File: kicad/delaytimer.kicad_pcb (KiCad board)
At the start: 2 copper layers, 39.6 x 33.3 mm, 21 parts, among them P1 CONN_01X04, Q1 MMBT3904, Q2 MMBT3904, Q3 MMBT3906, Q4 MMBT3906, Q5 IRLML6344, U1 NE555

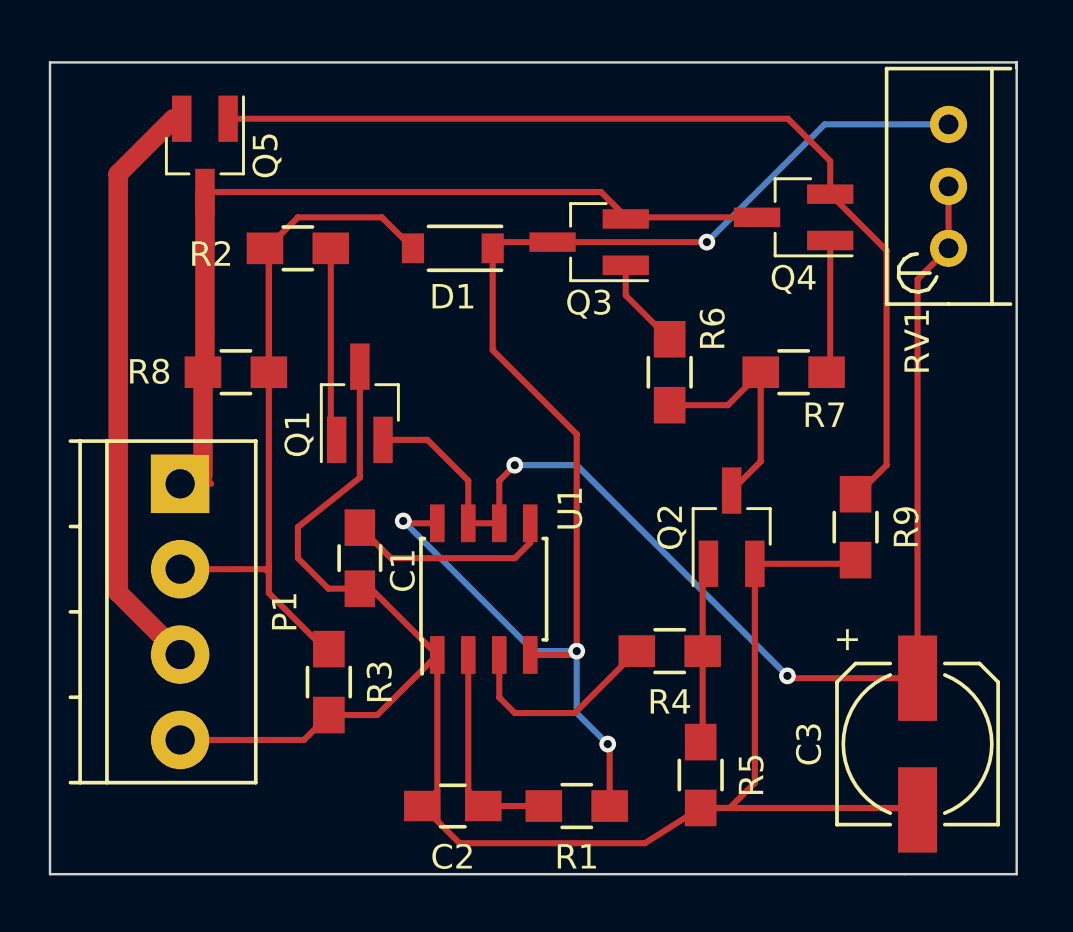
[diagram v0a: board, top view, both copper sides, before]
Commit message: Update schema / pcb / readme
- Removed unneeded resistor
- Reduce vias
- Fix labels for header
- Added copper pour on front/back
- UpdatedBOM
- Added Makefile for building BOM CSV
- Update README
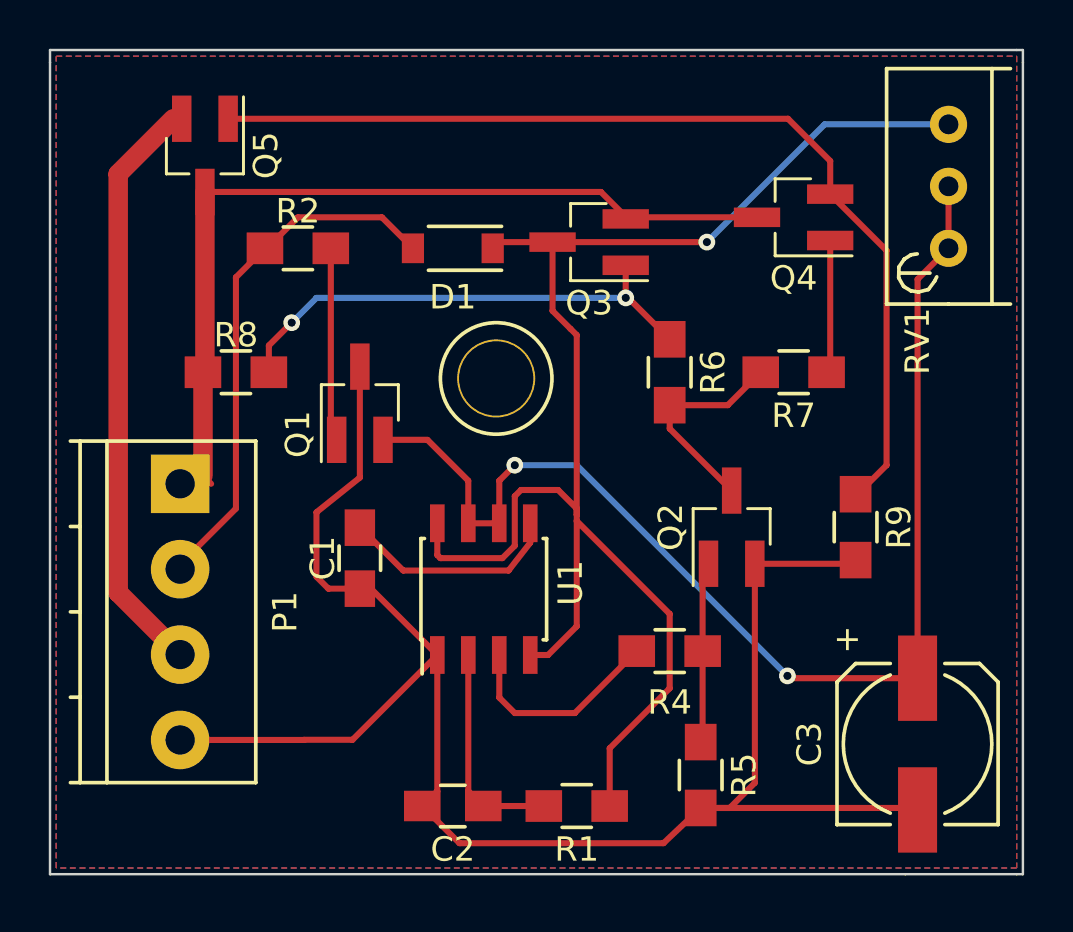
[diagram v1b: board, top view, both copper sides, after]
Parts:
- removed R3: 10k, Resistors_SMD:R_0805_HandSoldering
- added ?: , Connectors:1pin, F.Cu at (147.8, 93.0)
- R2: value 100k -> 2.2k
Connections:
- R8 pad 2: Switched12V -> Net-(Q3-Pad1)
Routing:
- net Net-(Q3-Pad1): track 3.78 -> 21.1 mm, vias 0 -> 2
- net Switched12V: track 33.6 -> 22.2 mm
- net VCC: track 59.2 -> 64.3 mm, vias 4 -> 1
- net Net-(Q2-Pad3): track 9.63 -> 8.84 mm
- net GND: track 72.1 -> 71.5 mm
- net Net-(C1-Pad1): track 8.56 -> 9.07 mm
- added copper zone on B.Cu, net GND
- added copper zone on F.Cu, net GND
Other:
- board size 39.6 x 33.3 mm -> 39.9 x 33.8 mm
- rule trace_min: 0.25 -> 0.1524
- board text added: "5-12V"
- board text added: "Output"
- board text added: "Switch"
- board text removed: "In12V"
- board text removed: "Out12V"
- board text removed: "Switch12V"

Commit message: Add static resistor option in place of pot
- Added a static resistor (ROpt) so you can save on the price of a pot
- Added measurements to the board for making an enclosure
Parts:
- added ROpt: 100k, Resistors_SMD:R_0805_HandSoldering, F.Cu at (160.3, 100.6)
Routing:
- net VCC: track 64.3 -> 75.5 mm
- net Net-(C3-Pad1): track 50.7 -> 54.1 mm
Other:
- board text added: "Ropt =Static Timer"
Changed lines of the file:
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@@
 (kicad_pcb (version 4) (host pcbnew 4.0.5)
   (general
-    (links 39)
-    (no_connects 0)
+    (links 43)
+    (no_connects 2)
     (area 129.489999 79.451999 169.468001 113.334001)
     (thickness 1.6002)
-    (drawings 14)
-    (tracks 135)
+    (drawings 24)
+    (tracks 142)
     (zones 0)
-    (modules 21)
+    (modules 22)
     (nets 16)
   )
@@
     (fp_line (start 3.302 -3.302) (end 3.302 -1.1176) (layer F.SilkS) (width 0.15))
     (fp_line (start -3.302 -2.54) (end -3.302 -1.1176) (layer F.SilkS) (width 0.15))
-    (fp_text user + (at -4.2799 2.9083 270) (layer F.SilkS)
+    (fp_text user + (at -4.572 -2.032 270) (layer F.SilkS)
       (effects (font (size 1 1) (thickness 0.15)))
     )
@@
     (pad 1 thru_hole circle (at 0 0) (size 3.2 3.2) (drill 3.048) (layers *.Cu *.Mask))
   )
+  (module Resistors_SMD:R_0805_HandSoldering (layer F.Cu)
+    (at 160.274 100.584 270)
+    (descr "Resistor SMD 0805, hand soldering")
+    (tags "resistor 0805")
+    (attr smd)
+    (fp_text reference ROpt (at 3.048 0 360) (layer F.SilkS)
+      (effects (font (size 1 1) (thickness 0.15)))
+    )
+    (fp_text value 100k (at 0 2.1 270) (layer F.Fab)
+      (effects (font (size 1 1) (thickness 0.15)))
+    )
+    (fp_line (start -1 0.625) (end -1 -0.625) (layer F.Fab) (width 0.1))
+    (fp_line (start 1 0.625) (end -1 0.625) (layer F.Fab) (width 0.1))
+    (fp_line (start 1 -0.625) (end 1 0.625) (layer F.Fab) (width 0.1))
+    (fp_line (start -1 -0.625) (end 1 -0.625) (layer F.Fab) (width 0.1))
+    (fp_line (start -2.4 -1) (end 2.4 -1) (layer F.CrtYd) (width 0.05))
+    (fp_line (start -2.4 1) (end 2.4 1) (layer F.CrtYd) (width 0.05))
+    (fp_line (start -2.4 -1) (end -2.4 1) (layer F.CrtYd) (width 0.05))
+    (fp_line (start 2.4 -1) (end 2.4 1) (layer F.CrtYd) (width 0.05))
+    (fp_line (start 0.6 0.875) (end -0.6 0.875) (layer F.SilkS) (width 0.15))
+    (fp_line (start -0.6 -0.875) (end 0.6 -0.875) (layer F.SilkS) (width 0.15))
+    (pad 1 smd rect (at -1.35 0 270) (size 1.5 1.3) (layers F.Cu F.Paste F.Mask)
+      (net 5 VCC))
+    (pad 2 smd rect (at 1.35 0 270) (size 1.5 1.3) (layers F.Cu F.Paste F.Mask)
+      (net 4 "Net-(C3-Pad1)"))
+    (model Resistors_SMD.3dshapes/R_0805_HandSoldering.wrl
+      (at (xyz 0 0 0))
+      (scale (xyz 1 1 1))
+      (rotate (xyz 0 0 0))
+    )
+  )
+  (dimension 13.97 (width 0.3) (layer Cmts.User)
+    (gr_text "13.970 mm" (at 117.268 102.489 90) (layer Cmts.User)
+      (effects (font (size 1.5 1.5) (thickness 0.3)))
+    )
+    (feature1 (pts (xy 135.382 95.504) (xy 115.918 95.504)))
+    (feature2 (pts (xy 135.382 109.474) (xy 115.918 109.474)))
+    (crossbar (pts (xy 118.618 109.474) (xy 118.618 95.504)))
+    (arrow1a (pts (xy 118.618 95.504) (xy 119.204421 96.630504)))
+    (arrow1b (pts (xy 118.618 95.504) (xy 118.031579 96.630504)))
+    (arrow2a (pts (xy 118.618 109.474) (xy 119.204421 108.347496)))
+    (arrow2b (pts (xy 118.618 109.474) (xy 118.031579 108.347496)))
+  )
+  (dimension 3.81 (width 0.3) (layer Cmts.User)
+    (gr_text "3.810 mm" (at 122.348 111.379 270) (layer Cmts.User)
+      (effects (font (size 1.5 1.5) (thickness 0.3)))
+    )
+    (feature1 (pts (xy 134.62 113.284) (xy 120.998 113.284)))
+    (feature2 (pts (xy 134.62 109.474) (xy 120.998 109.474)))
+    (crossbar (pts (xy 123.698 109.474) (xy 123.698 113.284)))
+    (arrow1a (pts (xy 123.698 113.284) (xy 123.111579 112.157496)))
+    (arrow1b (pts (xy 123.698 113.284) (xy 124.284421 112.157496)))
+    (arrow2a (pts (xy 123.698 109.474) (xy 123.111579 110.600504)))
+    (arrow2b (pts (xy 123.698 109.474) (xy 124.284421 110.600504)))
+  )
+  (gr_line (start 160.274 98.044) (end 159.766 97.79) (layer F.SilkS) (width 0.2))
+  (gr_line (start 160.782 97.79) (end 160.274 98.044) (layer F.SilkS) (width 0.2))
+  (gr_line (start 160.274 96.774) (end 160.274 98.044) (layer F.SilkS) (width 0.2))
+  (gr_text "Ropt =Static Timer" (at 160.274 96.012) (layer F.SilkS)
+    (effects (font (size 0.8 0.8) (thickness 0.1)))
+  )
+  (dimension 20.321587 (width 0.3) (layer Cmts.User)
+    (gr_text "20.322 mm" (at 178.761076 103.51225 89.28384005) (layer Cmts.User)
+      (effects (font (size 1.5 1.5) (thickness 0.3)))
+    )
+    (feature1 (pts (xy 147.574 113.284) (xy 179.983971 113.689124)))
+    (feature2 (pts (xy 147.828 92.964) (xy 180.237971 93.369124)))
+    (crossbar (pts (xy 177.538182 93.335377) (xy 177.284182 113.655377)))
+    (arrow1a (pts (xy 177.284182 113.655377) (xy 176.711887 112.521632)))
+    (arrow1b (pts (xy 177.284182 113.655377) (xy 177.884637 112.536291)))
+    (arrow2a (pts (xy 177.538182 93.335377) (xy 176.937727 94.454463)))
+    (arrow2b (pts (xy 177.538182 93.335377) (xy 178.110477 94.469122)))
+  )
+  (dimension 18.288 (width 0.3) (layer Cmts.User)
+    (gr_text "18.288 mm" (at 138.684 70.278) (layer Cmts.User)
+      (effects (font (size 1.5 1.5) (thickness 0.3)))
+    )
+    (feature1 (pts (xy 129.54 92.964) (xy 129.54 68.928)))
+    (feature2 (pts (xy 147.828 92.964) (xy 147.828 68.928)))
+    (crossbar (pts (xy 147.828 71.628) (xy 129.54 71.628)))
+    (arrow1a (pts (xy 129.54 71.628) (xy 130.666504 71.041579)))
+    (arrow1b (pts (xy 129.54 71.628) (xy 130.666504 72.214421)))
+    (arrow2a (pts (xy 147.828 71.628) (xy 146.701496 71.041579)))
+    (arrow2b (pts (xy 147.828 71.628) (xy 146.701496 72.214421)))
+  )
+  (dimension 33.782 (width 0.3) (layer Cmts.User)
+    (gr_text "33.782 mm" (at 173.562 96.393 270) (layer Cmts.User)
+      (effects (font (size 1.5 1.5) (thickness 0.3)))
+    )
+    (feature1 (pts (xy 169.418 113.284) (xy 174.912 113.284)))
+    (feature2 (pts (xy 169.418 79.502) (xy 174.912 79.502)))
+    (crossbar (pts (xy 172.212 79.502) (xy 172.212 113.284)))
+    (arrow1a (pts (xy 172.212 113.284) (xy 171.625579 112.157496)))
+    (arrow1b (pts (xy 172.212 113.284) (xy 172.798421 112.157496)))
+    (arrow2a (pts (xy 172.212 79.502) (xy 171.625579 80.628504)))
+    (arrow2b (pts (xy 172.212 79.502) (xy 172.798421 80.628504)))
+  )
+  (dimension 39.878 (width 0.3) (layer Cmts.User)
+    (gr_text "39.878 mm" (at 149.479 75.866) (layer Cmts.User)
+      (effects (font (size 1.5 1.5) (thickness 0.3)))
+    )
+    (feature1 (pts (xy 169.418 79.502) (xy 169.418 74.516)))
+    (feature2 (pts (xy 129.54 79.502) (xy 129.54 74.516)))
+    (crossbar (pts (xy 129.54 77.216) (xy 169.418 77.216)))
+    (arrow1a (pts (xy 169.418 77.216) (xy 168.291496 77.802421)))
+    (arrow1b (pts (xy 169.418 77.216) (xy 168.291496 76.629579)))
+    (arrow2a (pts (xy 129.54 77.216) (xy 130.666504 77.802421)))
+    (arrow2b (pts (xy 129.54 77.216) (xy 130.666504 76.629579)))
+  )
   (gr_line (start 169.418 113.284) (end 169.164 113.284) (angle 90) (layer Edge.Cuts) (width 0.1))
   (gr_line (start 169.164 79.502) (end 169.418 79.502) (angle 90) (layer Edge.Cuts) (width 0.1))
@@
   (segment (start 146.685 104.3) (end 146.685 109.875) (width 0.25) (layer F.Cu) (net 3))
   (segment (start 146.685 109.875) (end 147.3 110.49) (width 0.25) (layer F.Cu) (net 3))
+  (segment (start 160.274 101.934) (end 160.274 104.648) (width 0.25) (layer F.Cu) (net 4))
+  (segment (start 160.274 104.648) (end 159.766 105.156) (width 0.25) (layer F.Cu) (net 4))
   (segment (start 165.1 105.25) (end 159.86 105.25) (width 0.25) (layer F.Cu) (net 4))
   (segment (start 147.955 97.155) (end 147.955 98.9) (width 0.25) (layer F.Cu) (net 4))
@@
   (segment (start 165.1 105.25) (end 165.1 88.9) (width 0.25) (layer F.Cu) (net 4))
   (segment (start 165.1 88.9) (end 166.37 87.63) (width 0.25) (layer F.Cu) (net 4))
+  (segment (start 151.13 91.186) (end 151.13 94.234) (width 0.25) (layer F.Cu) (net 5))
+  (segment (start 151.13 94.234) (end 151.13 98.552) (width 0.25) (layer F.Cu) (net 5))
+  (segment (start 159.2 99.06) (end 155.956 99.06) (width 0.25) (layer F.Cu) (net 5))
+  (segment (start 155.956 99.06) (end 151.13 94.234) (width 0.25) (layer F.Cu) (net 5))
+  (segment (start 160.274 99.234) (end 159.374 99.234) (width 0.25) (layer F.Cu) (net 5))
+  (segment (start 159.374 99.234) (end 159.2 99.06) (width 0.25) (layer F.Cu) (net 5))
   (segment (start 145.415 98.9) (end 145.415 100.203) (width 0.25) (layer F.Cu) (net 5))
   (segment (start 151.13 98.298) (end 151.13 98.552) (width 0.25) (layer F.Cu) (net 5))
@@
   (segment (start 147.685 87.63) (end 147.685 87.741) (width 0.25) (layer F.Cu) (net 5))
   (segment (start 150.876 90.932) (end 151.13 91.186) (width 0.25) (layer F.Cu) (net 5))
-  (segment (start 151.13 91.186) (end 151.13 98.552) (width 0.25) (layer F.Cu) (net 5))
   (segment (start 151.13 98.552) (end 151.13 98.806) (width 0.25) (layer F.Cu) (net 5))
   (segment (start 151.13 98.806) (end 151.13 103.124) (width 0.25) (layer F.Cu) (net 5))

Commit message: Update to v1.1
- Fix Q1,Q4 which were connected wrong
- Fix routing of GND to use GND plane
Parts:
- renumbered ROpt to ROpt1
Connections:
- Q1 pad 2: Net-(C3-Pad1) -> GND
- Q1 pad 3: GND -> Net-(C3-Pad1)
- Q4 pad 2: Net-(Q4-Pad2) -> +12V
- Q4 pad 3: +12V -> Net-(Q4-Pad3)
- Q5 pad 1: Net-(Q4-Pad2) -> Net-(Q4-Pad3)
- R9 pad 1: Net-(Q4-Pad2) -> Net-(Q4-Pad3)
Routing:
- net GND: track 71.5 -> 0.00 mm
- net Net-(Q4-Pad3): track 0.00 -> 41.4 mm
- net Net-(Q4-Pad2): track 40.6 -> 0.00 mm
- net +12V: track 36.0 -> 40.1 mm
- net Net-(C3-Pad1): track 54.1 -> 57.0 mm
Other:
- board text added: "5-16V"
- board text added: "DelayTimer v1.1 https://synfin.net/delaytimer"
- board text added: "Ropt1=Static Timer"
- board text removed: "5-12V"
- board text removed: "DelayTimer v1.0 https://synfin.net/delaytimer"
- board text removed: "Ropt =Static Timer"
